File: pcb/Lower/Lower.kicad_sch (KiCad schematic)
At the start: 32 parts, among them J1 AudioJack3, J2 AudioJack3, J3 Barrel_Jack, J4 Conn_01x04, Q1 AO3401A, SW1 SW_Push_3PDT, U1 TL072

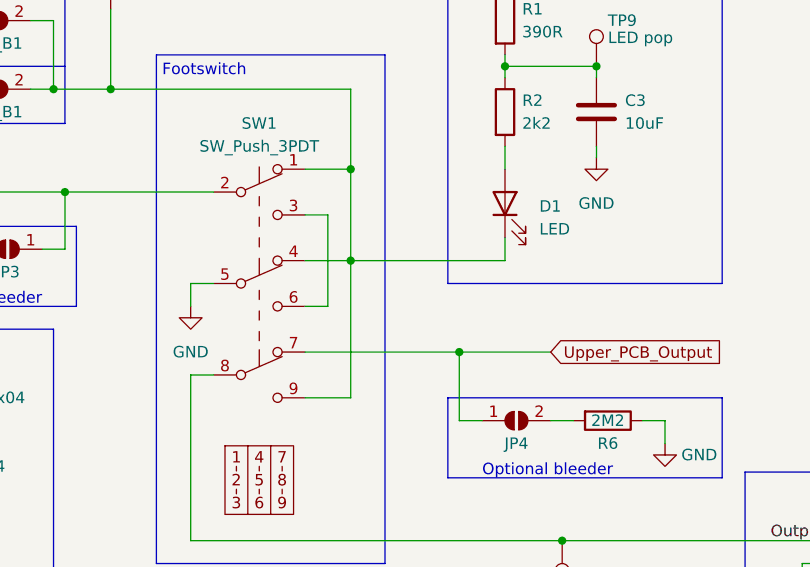
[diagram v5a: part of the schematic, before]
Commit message: [Lower] Fix LED wiring in Schematic, route whole board
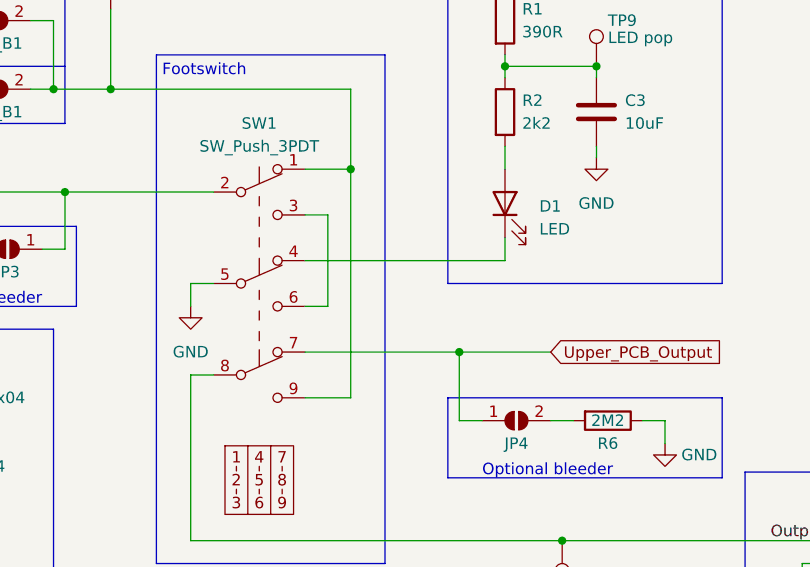
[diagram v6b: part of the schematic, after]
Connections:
- net at JP1_B1.2 (B), JP2_B1.2 (B), SW1.1 (A)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: no longer D1.1 (K), SW1.4 (A)
- new net: D1.1 (K), SW1.4 (A)
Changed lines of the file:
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@@
   (junction (at 161.29 101.6) (diameter 0) (color 0 0 0 0)
-  )
-  (junction (at 193.04 109.22) (diameter 0) (color 0 0 0 0)
   )
   (junction (at 205.105 119.38) (diameter 0) (color 0 0 0 0)
@@
     (stroke (width 0) (type default) (color 0 0 0 0))
   )
-  (wire (pts (xy 193.04 109.22) (xy 187.96 109.22))
-    (stroke (width 0) (type default) (color 0 0 0 0))
-  )
   (wire (pts (xy 81.28 90.17) (xy 83.82 90.17))
     (stroke (width 0) (type default) (color 0 0 0 0))
   )
-  (wire (pts (xy 193.04 109.22) (xy 193.04 124.46))
+  (wire (pts (xy 193.04 99.06) (xy 193.04 124.46))
     (stroke (width 0) (type default) (color 0 0 0 0))
   )
@@
     (stroke (width 0) (type default) (color 0 0 0 0))
   )
-  (wire (pts (xy 193.04 109.22) (xy 210.185 109.22))
+  (wire (pts (xy 187.96 109.22) (xy 210.185 109.22))
     (stroke (width 0) (type default) (color 0 0 0 0))
   )
@@
     (stroke (width 0) (type default) (color 0 0 0 0))
   )
-  (wire (pts (xy 193.04 99.06) (xy 193.04 109.22))
-    (stroke (width 0) (type default) (color 0 0 0 0))
-  )

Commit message: [Lower] Minor update to schematic BOM before ordering
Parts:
- U1: LCSC (none) -> C6961
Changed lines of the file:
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@@
       (effects (font (size 1.27 1.27)) hide)
     )
-    (property "Datasheet" "C6961" (id 3) (at 90.424 58.928 0)
+    (property "Datasheet" "" (id 3) (at 90.424 58.928 0)
+      (effects (font (size 1.27 1.27)) hide)
+    )
+    (property "LCSC" "C6961" (id 4) (at 90.424 58.928 0)
       (effects (font (size 1.27 1.27)) hide)
     )
@@
       (effects (font (size 1.27 1.27)) hide)
     )
-    (property "Datasheet" "C6961" (id 3) (at 124.46 72.39 0)
+    (property "Datasheet" "" (id 3) (at 124.46 72.39 0)
+      (effects (font (size 1.27 1.27)) hide)
+    )
+    (property "LCSC" "C6961" (id 4) (at 124.46 72.39 0)
       (effects (font (size 1.27 1.27)) hide)
     )
@@
       (effects (font (size 1.27 1.27)) hide)
     )
-    (property "Datasheet" "C6961" (id 3) (at 124.46 72.39 0)
-      (effects (font (size 1.27 1.27)) hide)
-    )
+    (property "Datasheet" "" (id 3) (at 124.46 72.39 0)
+      (effects (font (size 1.27 1.27)) hide)
+    )
+    (property "LCSC" "C6961" (id 4) (at 124.46 72.39 0)
+      (effects (font (size 1.27 1.27)) hide)
+    )
